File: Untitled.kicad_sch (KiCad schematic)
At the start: 4 parts, among them SW1 SW_Push

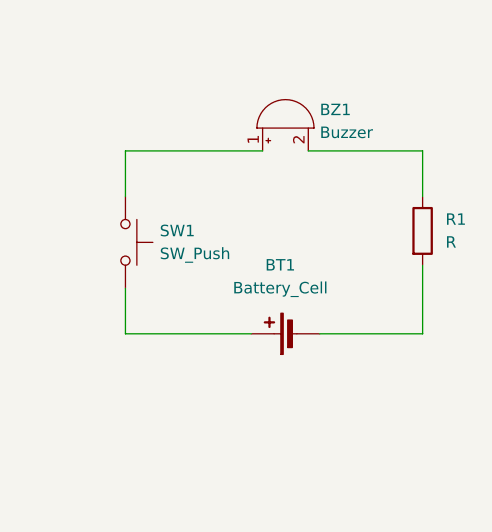
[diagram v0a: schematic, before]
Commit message: Added LEDs
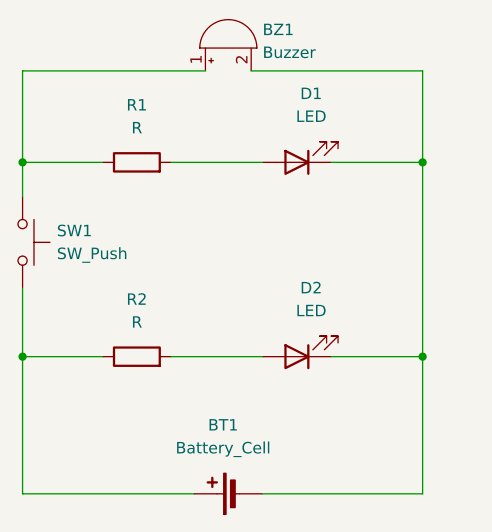
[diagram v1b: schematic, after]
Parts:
- added D1, D2: LED, LED_THT:LED_D5.0mm, symbol Device:LED
- added R2: R, Resistor_THT:R_Axial_DIN0207_L6.3mm_D2.5mm_P7.62mm_Horizontal, symbol Device:R
- BZ1: footprint Buzzer_Beeper:PUIAudio_SMT_0825_S_4_R -> Buzzer_Beeper:Buzzer_12x9.5RM7.6
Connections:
- net at BT1.1 (+), SW1.2: now also R2.1
- net at BT1.2 (-): now also BZ1.2 (-), D1.1 (K), D2.1 (K); no longer R1.2
- net at BZ1.1 (+), SW1.1: now also R1.1
- new net: D1.2 (A), R1.2
- new net: D2.2 (A), R2.2
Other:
- moved on the sheet: BT1, BZ1, SW1
